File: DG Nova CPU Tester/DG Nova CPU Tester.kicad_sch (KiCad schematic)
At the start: 122 parts, among them J1 Slot_02x50_Odd_Even, J10 Programmed I/O, J11 CPU Option Inputs, J12 Data Channel, J13 Program Interrupt, J14 System Control, J17 CPU Option Outputs, J18 MEM Control Outputs, J19 Logic 8 CH, J20 Logic 8 CH, J21 Arduino Anolog Pins, J22 Arduino Digital Pins, J23 Arduino Digital Pins, J4 ATX Power Port, J6 MBO, J7 MEM, J8 Data Channel, J9 Front Panel Controls, SW1 Arduino Mega Reset, SW1 Pico Reset, SW2 Power Swtich, U1 74HC14, U2 Pico

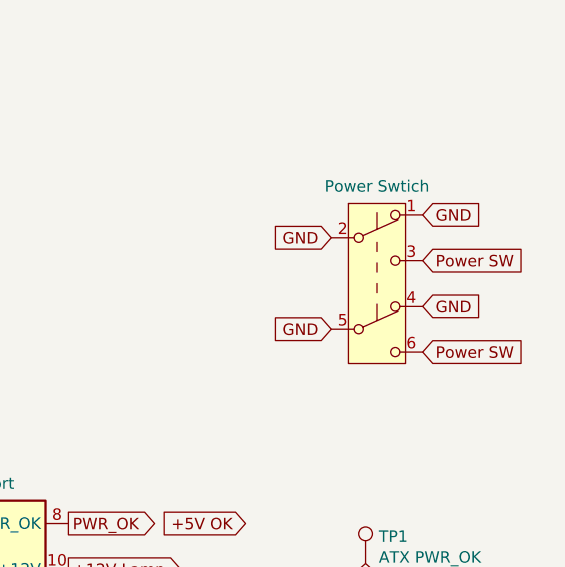
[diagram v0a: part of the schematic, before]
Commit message: atx fix
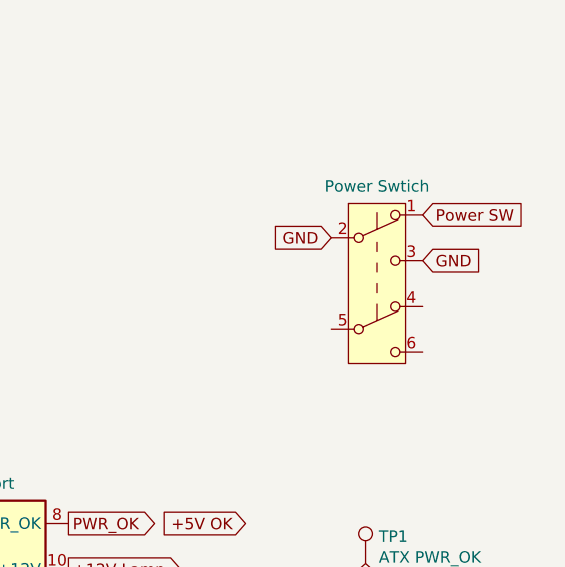
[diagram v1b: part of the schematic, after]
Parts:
- SW2: footprint Button_Switch_THT:SW_E-Switch_EG1271_SPDT -> Button_Switch_THT:SW_E-Switch_EG1224_SPDT_Angled
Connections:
- net GND: now also SW2.3 (C); no longer SW2.1 (A), SW2.4 (A), SW2.5 (B)
- net Power SW: now also SW2.1 (A); no longer SW2.3 (C), SW2.6 (C)
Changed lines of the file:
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@@
     )
   )
-  (global_label "GND" (shape input) (at 438.785 42.545 0) (fields_autoplaced)
-    (effects (font (size 1.27 1.27)) (justify left))
-    (property "Intersheetrefs" "${INTERSHEET_REFS}" (at 444.9865 42.545 0)
-      (effects (font (size 1.27 1.27)) (justify left) hide)
-    )
-  )
   (global_label "~{CON INST}" (shape input) (at 103.505 323.85 270) (fields_autoplaced)
     (effects (font (size 1.27 1.27)) (justify right))
@@
     )
   )
-  (global_label "Power SW" (shape input) (at 438.785 47.625 0) (fields_autoplaced)
-    (effects (font (size 1.27 1.27)) (justify left))
-    (property "Intersheetrefs" "${INTERSHEET_REFS}" (at 450.3688 47.625 0)
-      (effects (font (size 1.27 1.27)) (justify left) hide)
-    )
-  )
   (global_label "~{MBO2}" (shape input) (at 60.96 27.94 180) (fields_autoplaced)
     (effects (font (size 1.27 1.27)) (justify right))
@@
     )
   )
-  (global_label "GND" (shape input) (at 438.785 32.385 0) (fields_autoplaced)
+  (global_label "GND" (shape input) (at 438.785 37.465 0) (fields_autoplaced)
     (effects (font (size 1.27 1.27)) (justify left))
-    (property "Intersheetrefs" "${INTERSHEET_REFS}" (at 444.9865 32.385 0)
+    (property "Intersheetrefs" "${INTERSHEET_REFS}" (at 444.9865 37.465 0)
       (effects (font (size 1.27 1.27)) (justify left) hide)
     )
@@
     )
   )
-  (global_label "GND" (shape input) (at 428.625 45.085 180) (fields_autoplaced)
-    (effects (font (size 1.27 1.27)) (justify right))
-    (property "Intersheetrefs" "${INTERSHEET_REFS}" (at 422.4235 45.085 0)
-      (effects (font (size 1.27 1.27)) (justify right) hide)
-    )
-  )
   (global_label "~{MBO15}" (shape input) (at 55.245 233.045 0) (fields_autoplaced)
     (effects (font (size 1.27 1.27)) (justify left))
@@
     )
   )
-  (global_label "Power SW" (shape input) (at 438.785 37.465 0) (fields_autoplaced)
+  (global_label "Power SW" (shape input) (at 438.785 32.385 0) (fields_autoplaced)
     (effects (font (size 1.27 1.27)) (justify left))
-    (property "Intersheetrefs" "${INTERSHEET_REFS}" (at 450.3688 37.465 0)
+    (property "Intersheetrefs" "${INTERSHEET_REFS}" (at 450.3688 32.385 0)
       (effects (font (size 1.27 1.27)) (justify left) hide)
     )
@@
       (effects (font (size 1.27 1.27)))
     )
-    (property "Footprint" "Button_Switch_THT:SW_E-Switch_EG1271_SPDT" (at 433.705 34.925 0)
+    (property "Footprint" "Button_Switch_THT:SW_E-Switch_EG1224_SPDT_Angled" (at 433.705 34.925 0)
       (effects (font (size 1.27 1.27)) hide)
     )

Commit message: repairs
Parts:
- added SW4: SW_DIP_x04, Package_DIP:DIP-8_W7.62mm, symbol Switch:SW_DIP_x04
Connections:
- net GND: now also SW4.5, SW4.6, SW4.7, SW4.8
- net DIP1: now reaches J23.3 (Pin_3), XA1.D10
- net DIP1: now also SW4.1
- net DIP4: now reaches J22.5 (Pin_5), XA1.D7
- net DIP4: now also SW4.4
- net DIP3: now reaches J23.1 (Pin_1), XA1.D8
- net DIP3: now also SW4.3
- net DIP2: now reaches J23.2 (Pin_2), XA1.D9
- net DIP2: now also SW4.2
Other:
- moved on the sheet: J22, J23

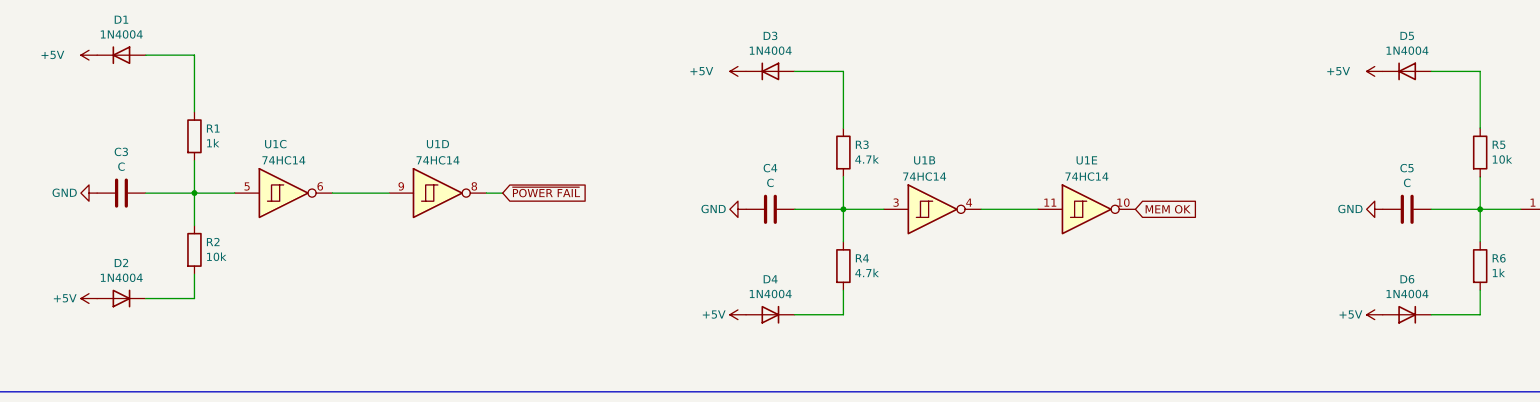
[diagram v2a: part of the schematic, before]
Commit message: 4.7uf polarized
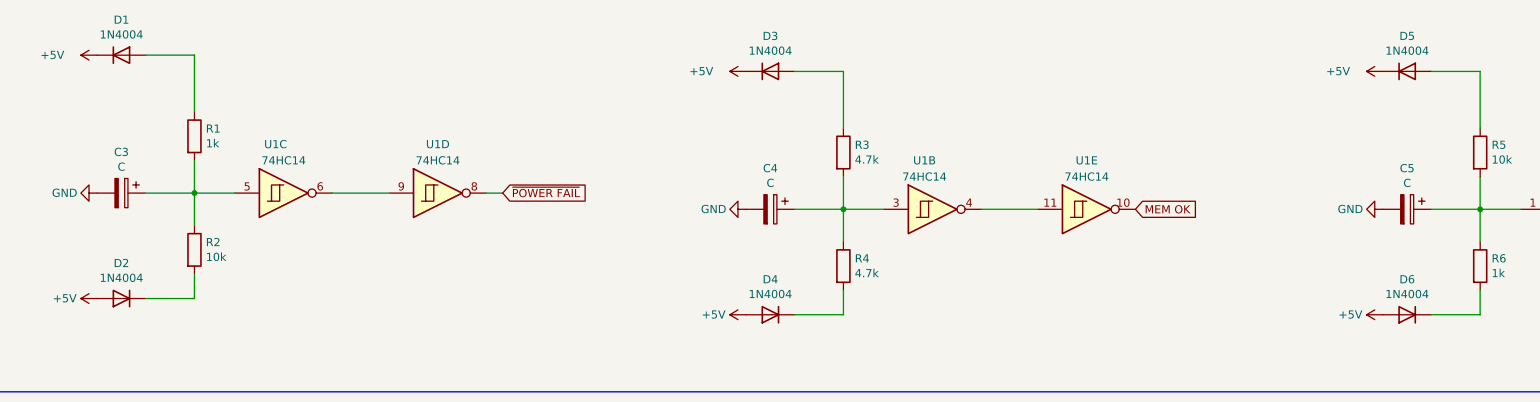
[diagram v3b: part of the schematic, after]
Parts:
- C3, C4, C5: footprint Capacitor_THT:C_Disc_D6.0mm_W2.5mm_P5.00mm -> Capacitor_THT:CP_Radial_D4.0mm_P2.00mm; symbol Device:C -> Device:C_Polarized
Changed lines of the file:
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@@
     )
   )
-  (symbol (lib_id "Device:C") (at 249.555 491.49 270) (unit 1)
+  (symbol (lib_id "Device:C_Polarized") (at 249.555 491.49 270) (unit 1)
     (in_bom yes) (on_board yes) (dnp no)
     (property "Reference" "C5" (at 249.555 485.0892 90)
@@
       (effects (font (size 1.27 1.27)))
     )
-    (property "Footprint" "Capacitor_THT:C_Disc_D6.0mm_W2.5mm_P5.00mm" (at 245.745 492.4552 0)
+    (property "Footprint" "Capacitor_THT:CP_Radial_D4.0mm_P2.00mm" (at 245.745 492.4552 0)
       (effects (font (size 1.27 1.27)) hide)
     )
@@
     )
   )
-  (symbol (lib_id "Device:C") (at 149.86 491.49 270) (unit 1)
+  (symbol (lib_id "Device:C_Polarized") (at 149.86 491.49 270) (unit 1)
     (in_bom yes) (on_board yes) (dnp no)
     (property "Reference" "C4" (at 149.86 485.0892 90)
@@
       (effects (font (size 1.27 1.27)))
     )
-    (property "Footprint" "Capacitor_THT:C_Disc_D6.0mm_W2.5mm_P5.00mm" (at 146.05 492.4552 0)
+    (property "Footprint" "Capacitor_THT:CP_Radial_D4.0mm_P2.00mm" (at 146.05 492.4552 0)
       (effects (font (size 1.27 1.27)) hide)
     )
@@
     )
   )
-  (symbol (lib_id "Device:C") (at 48.26 488.95 270) (unit 1)
+  (symbol (lib_id "Device:C_Polarized") (at 48.26 488.95 270) (unit 1)
     (in_bom yes) (on_board yes) (dnp no)
     (property "Reference" "C3" (at 48.26 482.5492 90)
@@
       (effects (font (size 1.27 1.27)))
     )
-    (property "Footprint" "Capacitor_THT:C_Disc_D6.0mm_W2.5mm_P5.00mm" (at 44.45 489.9152 0)
+    (property "Footprint" "Capacitor_THT:CP_Radial_D4.0mm_P2.00mm" (at 44.45 489.9152 0)
       (effects (font (size 1.27 1.27)) hide)
     )

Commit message: yeah
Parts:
- added U3, U4: 74LS08, Package_DIP:DIP-14_W7.62mm, symbol 74xx:74LS08
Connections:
- net +5V: now also U3.14 (VCC), U4.14 (VCC)
- net DIP1: now also SW4.4; no longer SW4.1
- net DIP2: now also SW4.3; no longer SW4.2
- net DIP3: now also SW4.2; no longer SW4.3
- net DIP4: now also SW4.1; no longer SW4.4
- net GND: now also U3.7 (GND), U4.7 (GND)
- net ~{CON INST}: now also U3.1, U3.12, U3.4, U3.9, U4.1, U4.12, U4.4, U4.9
- net ~{MEM0}: now also U3.3
- net ~{MEM1}: now also U3.6
- net ~{MEM2}: now also U3.8
- net ~{MEM3}: now also U3.11
- net ~{MEM4}: now also U4.3
- net ~{MEM5}: now also U4.6
- net ~{MEM6}: now also U4.8
- net ~{MEM7}: now also U4.11
- new net A08: U4.13
- new net A09: U4.10
- new net A10: U4.5
- new net A11: U4.2
- new net A12: U3.13
- new net A13: U3.10
- new net A14: U3.5
- new net A15: U3.2
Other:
- note added: "Front Panel MEM0-7 AND gates for speed"
- moved on the sheet: Teensy 4.1

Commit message: more mem
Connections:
- net D11: now reaches J23.4 (Pin_4), XA1.D11
- net D12: now reaches J23.5 (Pin_5), XA1.D12
- net D3: now reaches J22.1 (Pin_1), XA1.D3 (D3_INT1)
- net D4: now reaches J22.2 (Pin_2), XA1.D4
- net D5: now reaches J22.3 (Pin_3), XA1.D5
- net D6: now reaches J22.4 (Pin_4), XA1.D6
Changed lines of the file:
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@@
   )
   (text "https://forum.arduino.cc/t/arduino-mega-aref-sda-slc-iorf-5v/1218872"
-    (at 123.825 197.485 0)
+    (at 187.325 262.89 90)
     (effects (font (size 1.27 1.27)) (justify left bottom))
   )
@@
     (effects (font (size 1.27 1.27)) (justify left bottom))
   )
+  (label "D3" (at 226.695 169.545 0) (fields_autoplaced)
+    (effects (font (size 1.27 1.27)) (justify left bottom))
+  )
+  (label "D6" (at 226.695 177.165 0) (fields_autoplaced)
+    (effects (font (size 1.27 1.27)) (justify left bottom))
+  )
+  (label "D5" (at 226.695 174.625 0) (fields_autoplaced)
+    (effects (font (size 1.27 1.27)) (justify left bottom))
+  )
+  (label "D11" (at 226.06 189.865 0) (fields_autoplaced)
+    (effects (font (size 1.27 1.27)) (justify left bottom))
+  )
   (label "DIP2" (at 217.17 184.785 0) (fields_autoplaced)
+    (effects (font (size 1.27 1.27)) (justify left bottom))
+  )
+  (label "D4" (at 226.695 172.085 0) (fields_autoplaced)
     (effects (font (size 1.27 1.27)) (justify left bottom))
   )
@@
     (effects (font (size 1.27 1.27)) (justify left bottom))
   )
+  (label "D12" (at 226.06 192.405 0) (fields_autoplaced)
+    (effects (font (size 1.27 1.27)) (justify left bottom))
+  )

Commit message: go
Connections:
- net +5V OK: no longer J23.6 (Pin_6), XA1.D13
- net D11 renamed ClockPin2
- net D12 renamed LatchPin2
- net D3 renamed DataPin1
- net D4 renamed ClockPin1
- net D5 renamed LatchPin1
- net D6 renamed DataPin2
- new net: J23.6 (Pin_6), XA1.D13
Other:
- note added: "Previously +5v OK but that caused problems so I cut the trace"
- note added: "Used by Piggyback MEM0-7 + Addr board"
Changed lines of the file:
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@@
+    (fill (type none))
+  )
+  (rectangle (start 111.125 218.44) (end 125.095 239.395)
+    (stroke (width 0) (type default))
     (fill (type none))
   )
@@
     (effects (font (size 1.27 1.27) (thickness 0.254) bold) (justify right bottom))
   )
+  (text "Used by \nPiggyback MEM0-7 + Addr\nboard" (at 116.205 238.76 90)
+    (effects (font (size 1 1)) (justify left bottom))
+  )
+  (text "Previously +5v OK\nbut that caused problems\nso I cut the trace\n"
+    (at 225.425 197.485 0)
+    (effects (font (size 0.5 0.5)) (justify left bottom))
+  )
   (text "Address 15 light" (at 64.135 233.68 0)
     (effects (font (size 0.9906 0.9906)) (justify left bottom))
@@
     (effects (font (size 1.27 1.27)) (justify left bottom))
   )
-  (label "D3" (at 226.695 169.545 0) (fields_autoplaced)
-    (effects (font (size 1.27 1.27)) (justify left bottom))
-  )
-  (label "D6" (at 226.695 177.165 0) (fields_autoplaced)
-    (effects (font (size 1.27 1.27)) (justify left bottom))
-  )
-  (label "D5" (at 226.695 174.625 0) (fields_autoplaced)
-    (effects (font (size 1.27 1.27)) (justify left bottom))
-  )
-  (label "D11" (at 226.06 189.865 0) (fields_autoplaced)
+  (label "DataPin1" (at 220.98 169.545 0) (fields_autoplaced)
+    (effects (font (size 1.27 1.27)) (justify left bottom))
+  )
+  (label "DataPin2" (at 220.98 177.165 0) (fields_autoplaced)
+    (effects (font (size 1.27 1.27)) (justify left bottom))
+  )
+  (label "LatchPin1" (at 220.98 174.625 0) (fields_autoplaced)
+    (effects (font (size 1.27 1.27)) (justify left bottom))
+  )
+  (label "ClockPin2" (at 220.345 189.865 0) (fields_autoplaced)
     (effects (font (size 1.27 1.27)) (justify left bottom))
   )
@@
     (effects (font (size 1.27 1.27)) (justify left bottom))
   )
-  (label "D4" (at 226.695 172.085 0) (fields_autoplaced)
+  (label "ClockPin1" (at 220.98 172.085 0) (fields_autoplaced)
     (effects (font (size 1.27 1.27)) (justify left bottom))
   )
@@
     (effects (font (size 1.27 1.27)) (justify left bottom))
   )
-  (label "D12" (at 226.06 192.405 0) (fields_autoplaced)
-    (effects (font (size 1.27 1.27)) (justify left bottom))
-  )
-  (label "+5V OK" (at 221.615 194.945 0) (fields_autoplaced)
-    (effects (font (size 1.27 1.27)) (justify left bottom))
-  )
+  (label "LatchPin2" (at 220.345 192.405 0) (fields_autoplaced)
+    (effects (font (size 1.27 1.27)) (justify left bottom))
+  )

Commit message: Lots o updates
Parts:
- removed unit 2 of U3
- removed unit 1 of U3
- removed unit 3 of U3
- removed unit 4 of U3
- removed unit 4 of U4
- removed unit 3 of U4
- removed unit 2 of U4
- removed unit 1 of U4
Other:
- note removed: "Front Panel MEM0-7 AND gates for speed"

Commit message: KiCad 9 and LED Buffers!
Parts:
- removed U3, U4: 74LS08, Package_DIP:DIP-14_W7.62mm, symbol 74xx:74LS08
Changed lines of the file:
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@@
     )
   )
-  (global_label "GND" (shape input) (at 36.195 568.96 270) (fields_autoplaced)
-    (effects (font (size 1.27 1.27)) (justify right))
-    (property "Intersheetrefs" "${INTERSHEET_REFS}" (at 36.195 575.7363 90)
-      (effects (font (size 1.27 1.27)) (justify right) hide)
-    )
-  )
   (global_label "~{MEM15}" (shape input) (at 42.545 159.385 180) (fields_autoplaced)
     (effects (font (size 1.27 1.27)) (justify right))
@@
     )
   )
-  (global_label "+5V" (shape input) (at 61.595 543.56 90) (fields_autoplaced)
-    (effects (font (size 1.27 1.27)) (justify left))
-    (property "Intersheetrefs" "${INTERSHEET_REFS}" (at 61.595 536.7837 90)
-      (effects (font (size 1.27 1.27)) (justify left) hide)
-    )
-  )
   (global_label "GND After Meter" (shape output) (at 352.425 44.45 270) (fields_autoplaced)
     (effects (font (size 1.27 1.27)) (justify right))
@@
     )
   )
-  (global_label "+5V" (shape input) (at 36.195 543.56 90) (fields_autoplaced)
-    (effects (font (size 1.27 1.27)) (justify left))
-    (property "Intersheetrefs" "${INTERSHEET_REFS}" (at 36.195 536.7837 90)
-      (effects (font (size 1.27 1.27)) (justify left) hide)
-    )
-  )
   (global_label "~{DATA15}" (shape input) (at 293.37 415.925 270) (fields_autoplaced)
     (effects (font (size 1.27 1.27)) (justify right))
@@
     )
   )
-  (global_label "GND" (shape input) (at 61.595 568.96 270) (fields_autoplaced)
-    (effects (font (size 1.27 1.27)) (justify right))
-    (property "Intersheetrefs" "${INTERSHEET_REFS}" (at 61.595 575.7363 90)
-      (effects (font (size 1.27 1.27)) (justify right) hide)
-    )
-  )
   (global_label "+5V OK" (shape input) (at 228.6 62.23 180) (fields_autoplaced)
     (effects (font (size 1.27 1.27)) (justify right))
@@
     )
   )
-  (symbol (lib_id "74xx:74LS08") (at 36.195 556.26 0) (unit 5)
-    (in_bom yes) (on_board yes) (dnp no) (fields_autoplaced)
-    (property "Reference" "U3" (at 42.037 555.6163 0)
-      (effects (font (size 1.27 1.27)) (justify left))
-    )
-    (property "Value" "74LS08" (at 42.037 557.5373 0)
-      (effects (font (size 1.27 1.27)) (justify left))
-    )
-    (property "Footprint" "Package_DIP:DIP-14_W7.62mm" (at 36.195 556.26 0)
-      (effects (font (size 1.27 1.27)) hide)
-    )
-    (property "Datasheet" "http://www.ti.com/lit/gpn/sn74LS08" (at 36.195 556.26 0)
-      (effects (font (size 1.27 1.27)) hide)
-    )
-    (pin "1")
-    (pin "2")
-    (pin "3")
-    (pin "4")
-    (pin "5")
-    (pin "6")
-    (pin "10")
-    (pin "8")
-    (pin "9")
-    (pin "11")
-    (pin "12")
-    (pin "13")
-    (pin "14")
-    (pin "7")
-    (instances
-      (project "DG Nova CPU Tester"
-        (path "/c1f710ce-b3f9-4828-9325-9c2326e8d74c"
-          (reference "U3") (unit 5)
-        )
-      )
-      (project "Piggyback MEM0-7"
-        (path "/fe0be92e-1d85-43cc-bb82-88d36766eebc"
-          (reference "U2") (unit 5)
-        )
-      )
-    )
-  )
   (symbol (lib_id "Device:LED") (at 208.915 -21.59 0) (unit 1)
     (in_bom yes) (on_board yes) (dnp no)
@@
         )
       )
-    )
-  )
-  (symbol (lib_id "74xx:74LS08") (at 61.595 556.26 0) (unit 5)
-    (in_bom yes) (on_board yes) (dnp no) (fields_autoplaced)
-    (property "Reference" "U4" (at 67.437 555.6163 0)
-      (effects (font (size 1.27 1.27)) (justify left))
-    )
-    (property "Value" "74LS08" (at 67.437 557.5373 0)
-      (effects (font (size 1.27 1.27)) (justify left))
-    )
-    (property "Footprint" "Package_DIP:DIP-14_W7.62mm" (at 61.595 556.26 0)
-      (effects (font (size 1.27 1.27)) hide)
-    )
-    (property "Datasheet" "http://www.ti.com/lit/gpn/sn74LS08" (at 61.595 556.26 0)
-      (effects (font (size 1.27 1.27)) hide)
-    )
-    (pin "1")
-    (pin "2")
-    (pin "3")
-    (pin "4")
-    (pin "5")
-    (pin "6")
-    (pin "10")
-    (pin "8")
-    (pin "9")
-    (pin "11")
-    (pin "12")
-    (pin "13")
-    (pin "14")
-    (pin "7")
-    (instances
-      (project "DG Nova CPU Tester"
-        (path "/c1f710ce-b3f9-4828-9325-9c2326e8d74c"
-          (reference "U4") (unit 5)
-        )
-      )
-      (project "Piggyback MEM0-7"
-        (path "/fe0be92e-1d85-43cc-bb82-88d36766eebc"
-          (reference "U3") (unit 5)
-        )
-      )
